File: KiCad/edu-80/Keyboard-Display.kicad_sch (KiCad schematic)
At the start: 69 parts, among them Q10 ED1602, Q11 ED1602, Q12 ED1602, Q13 ED1602, Q14 ED1602, Q15 ED1602, Q16 ED1602, Q17 ED1602, Q18 ED1602, Q19 ED1602, Q20 ED1602, Q4 ED1602, Q5 ED1602, Q6 ED1602, Q7 ED1602, Q8 ED1602, Q9 ED1602, U9 7442

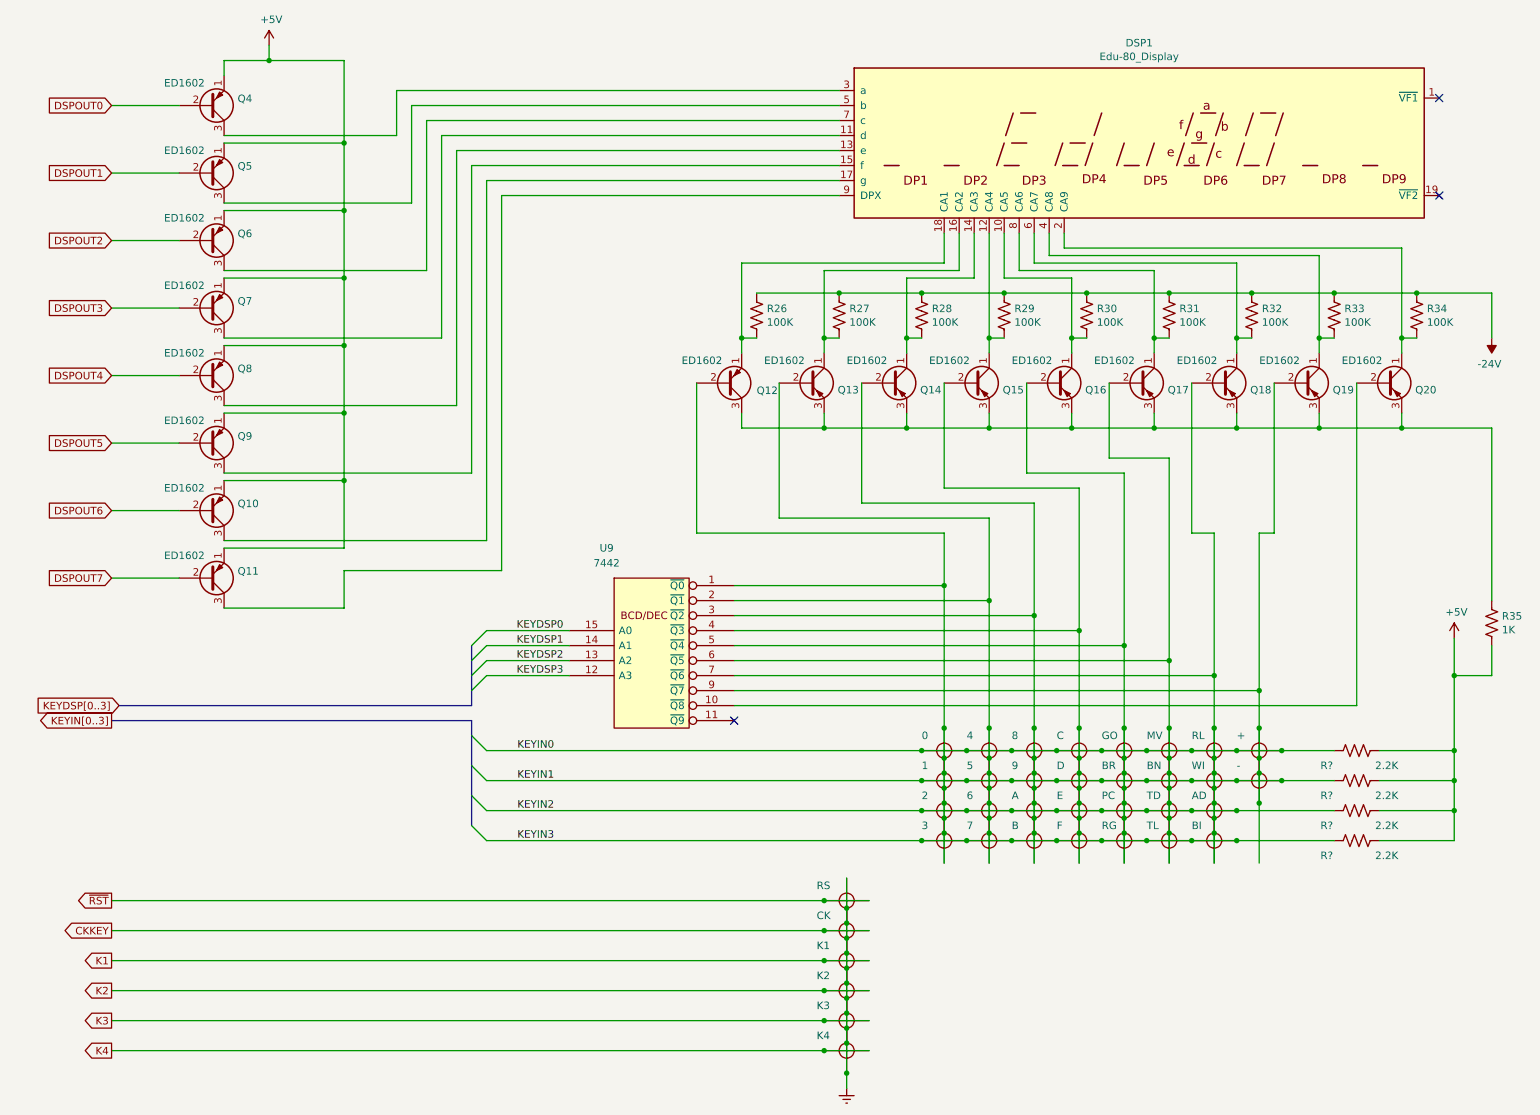
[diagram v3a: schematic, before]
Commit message: Fixed ~IRQ vs. INT for PIO/CTC. Removed old (version 5) schematic files.
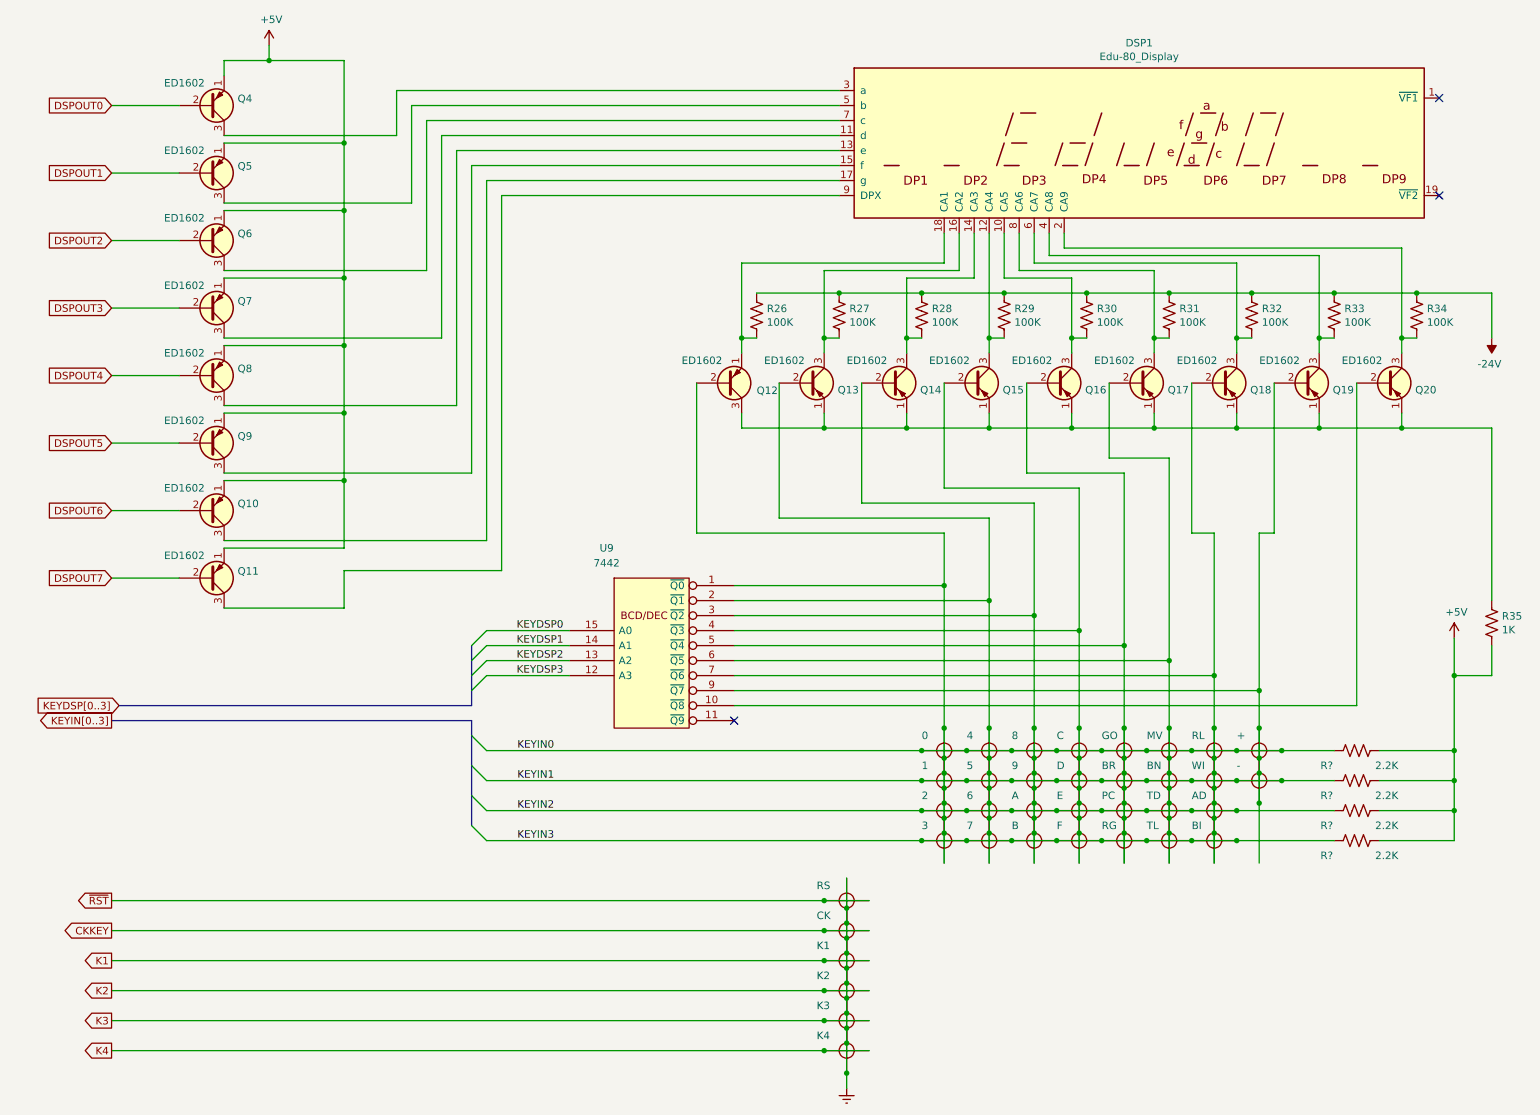
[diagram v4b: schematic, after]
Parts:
- Q10, Q11, Q12, Q4, Q5, Q6, Q7, Q8, Q9: symbol Device:Q_PNP_EBC -> Edu-80_Symbols:Q_PNP_EBC
- Q13, Q14, Q15, Q16, Q17, Q18, Q19, Q20: symbol Device:Q_PNP_CBE -> Edu-80_Symbols:Q_PNP_EBC
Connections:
- net at DSP1.8 (CA6), R31.2: now also Q17.3 (C); no longer Q17.1 (C)
- net at DSP1.6 (CA7), R32.2: now also Q18.3 (C); no longer Q18.1 (C)
- net at DSP1.4 (CA8), R33.2: now also Q19.3 (C); no longer Q19.1 (C)
- net at DSP1.2 (CA9), R34.2: now also Q20.3 (C); no longer Q20.1 (C)
- net at DSP1.10 (CA5), R30.2: now also Q16.3 (C); no longer Q16.1 (C)
- net at DSP1.12 (CA4), R29.2: now also Q15.3 (C); no longer Q15.1 (C)
- net at DSP1.14 (CA3), R28.2: now also Q14.3 (C); no longer Q14.1 (C)
- net at DSP1.16 (CA2), R27.2: now also Q13.3 (C); no longer Q13.1 (C)
- new net: Q12.3 (C), Q13.1 (E), Q14.1 (E), Q15.1 (E), Q16.1 (E), Q17.1 (E), Q18.1 (E), Q19.1 (E), Q20.1 (E), R35.1
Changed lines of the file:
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@@
   (title_block
     (title "Edu-80 Z80 Trainer")
-    (date "2023-06-03")
+    (date "2023-06-05")
     (rev "0.1")
     (company "Strangers")
-    (comment 1 "Author: James D. Tucker")
+    (comment 4 "Author: James D. Tucker")
   )
   (junction (at 187.96 85.09) (diameter 0) (color 0 0 0 0)
@@
     )
   )
-  (symbol (lib_id "Device:Q_PNP_CBE") (at 199.39 77.47 0) (unit 1)
+  (symbol (lib_id "Edu-80_Symbols:Q_PNP_EBC") (at 199.39 77.47 0) (unit 1)
     (in_bom yes) (on_board yes) (dnp no)
     (property "Reference" "Q17" (at 204.216 78.6384 0)
@@
     )
   )
-  (symbol (lib_id "Device:Q_PNP_CBE") (at 213.36 77.47 0) (unit 1)
+  (symbol (lib_id "Edu-80_Symbols:Q_PNP_EBC") (at 213.36 77.47 0) (unit 1)
     (in_bom yes) (on_board yes) (dnp no)
     (property "Reference" "Q18" (at 218.186 78.6384 0)
@@
     )
   )
-  (symbol (lib_id "Device:Q_PNP_CBE") (at 227.33 77.47 0) (unit 1)
+  (symbol (lib_id "Edu-80_Symbols:Q_PNP_EBC") (at 227.33 77.47 0) (unit 1)
     (in_bom yes) (on_board yes) (dnp no)
     (property "Reference" "Q19" (at 232.156 78.6384 0)
@@
     )
   )
-  (symbol (lib_id "Device:Q_PNP_CBE") (at 241.3 77.47 0) (unit 1)
+  (symbol (lib_id "Edu-80_Symbols:Q_PNP_EBC") (at 241.3 77.47 0) (unit 1)
     (in_bom yes) (on_board yes) (dnp no)
     (property "Reference" "Q20" (at 246.126 78.6384 0)
@@
     )
   )
-  (symbol (lib_id "Device:Q_PNP_EBC") (at 41.91 30.48 0) (mirror x) (unit 1)
+  (symbol (lib_id "Edu-80_Symbols:Q_PNP_EBC") (at 41.91 30.48 0) (mirror x) (unit 1)
     (in_bom yes) (on_board yes) (dnp no)
     (property "Reference" "Q4" (at 46.736 29.3116 0)
@@
     )
   )
-  (symbol (lib_id "Device:Q_PNP_EBC") (at 41.91 41.91 0) (mirror x) (unit 1)
+  (symbol (lib_id "Edu-80_Symbols:Q_PNP_EBC") (at 41.91 41.91 0) (mirror x) (unit 1)
     (in_bom yes) (on_board yes) (dnp no)
     (property "Reference" "Q5" (at 46.736 40.7416 0)
@@
     )
   )
-  (symbol (lib_id "Device:Q_PNP_EBC") (at 41.91 53.34 0) (mirror x) (unit 1)
+  (symbol (lib_id "Edu-80_Symbols:Q_PNP_EBC") (at 41.91 53.34 0) (mirror x) (unit 1)
     (in_bom yes) (on_board yes) (dnp no)
     (property "Reference" "Q6" (at 46.736 52.1716 0)
@@
     )
   )
-  (symbol (lib_id "Device:Q_PNP_EBC") (at 41.91 64.77 0) (mirror x) (unit 1)
+  (symbol (lib_id "Edu-80_Symbols:Q_PNP_EBC") (at 41.91 64.77 0) (mirror x) (unit 1)
     (in_bom yes) (on_board yes) (dnp no)
     (property "Reference" "Q7" (at 46.736 63.6016 0)
@@
     )
   )
-  (symbol (lib_id "Device:Q_PNP_EBC") (at 41.91 76.2 0) (mirror x) (unit 1)
+  (symbol (lib_id "Edu-80_Symbols:Q_PNP_EBC") (at 41.91 76.2 0) (mirror x) (unit 1)
     (in_bom yes) (on_board yes) (dnp no)
     (property "Reference" "Q8" (at 46.736 75.0316 0)
@@
     )
   )
-  (symbol (lib_id "Device:Q_PNP_EBC") (at 41.91 87.63 0) (mirror x) (unit 1)
+  (symbol (lib_id "Edu-80_Symbols:Q_PNP_EBC") (at 41.91 87.63 0) (mirror x) (unit 1)
     (in_bom yes) (on_board yes) (dnp no)
     (property "Reference" "Q9" (at 46.736 86.4616 0)
@@
     )
   )
-  (symbol (lib_id "Device:Q_PNP_EBC") (at 41.91 99.06 0) (mirror x) (unit 1)
+  (symbol (lib_id "Edu-80_Symbols:Q_PNP_EBC") (at 41.91 99.06 0) (mirror x) (unit 1)
     (in_bom yes) (on_board yes) (dnp no)
     (property "Reference" "Q10" (at 46.736 97.8916 0)
@@
     )
   )
-  (symbol (lib_id "Device:Q_PNP_EBC") (at 41.91 110.49 0) (mirror x) (unit 1)
+  (symbol (lib_id "Edu-80_Symbols:Q_PNP_EBC") (at 41.91 110.49 0) (mirror x) (unit 1)
     (in_bom yes) (on_board yes) (dnp no)
     (property "Reference" "Q11" (at 46.736 109.3216 0)
@@
     )
   )
-  (symbol (lib_id "Device:Q_PNP_EBC") (at 129.54 77.47 0) (mirror x) (unit 1)
+  (symbol (lib_id "Edu-80_Symbols:Q_PNP_EBC") (at 129.54 77.47 0) (mirror x) (unit 1)
     (in_bom yes) (on_board yes) (dnp no)
     (property "Reference" "Q12" (at 134.62 78.74 0)
@@
     )
   )
-  (symbol (lib_id "Device:Q_PNP_CBE") (at 143.51 77.47 0) (unit 1)
+  (symbol (lib_id "Edu-80_Symbols:Q_PNP_EBC") (at 143.51 77.47 0) (unit 1)
     (in_bom yes) (on_board yes) (dnp no)
     (property "Reference" "Q13" (at 148.336 78.6384 0)
@@
     )
   )
-  (symbol (lib_id "Device:Q_PNP_CBE") (at 157.48 77.47 0) (unit 1)
+  (symbol (lib_id "Edu-80_Symbols:Q_PNP_EBC") (at 157.48 77.47 0) (unit 1)
     (in_bom yes) (on_board yes) (dnp no)
     (property "Reference" "Q14" (at 162.306 78.6384 0)
@@
     )
   )
-  (symbol (lib_id "Device:Q_PNP_CBE") (at 171.45 77.47 0) (unit 1)
+  (symbol (lib_id "Edu-80_Symbols:Q_PNP_EBC") (at 171.45 77.47 0) (unit 1)
     (in_bom yes) (on_board yes) (dnp no)
     (property "Reference" "Q15" (at 176.276 78.6384 0)
@@
     )
   )
-  (symbol (lib_id "Device:Q_PNP_CBE") (at 185.42 77.47 0) (unit 1)
+  (symbol (lib_id "Edu-80_Symbols:Q_PNP_EBC") (at 185.42 77.47 0) (unit 1)
     (in_bom yes) (on_board yes) (dnp no)
     (property "Reference" "Q16" (at 190.246 78.6384 0)
